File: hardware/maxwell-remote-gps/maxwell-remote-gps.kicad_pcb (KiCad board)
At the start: 2 copper layers, 52 x 21.5 mm, 11 parts, among them J1 IO, J2 UART1, U1 SC16IS752IPW, U2 FGPMMOPA6C, Y1 14.7456M

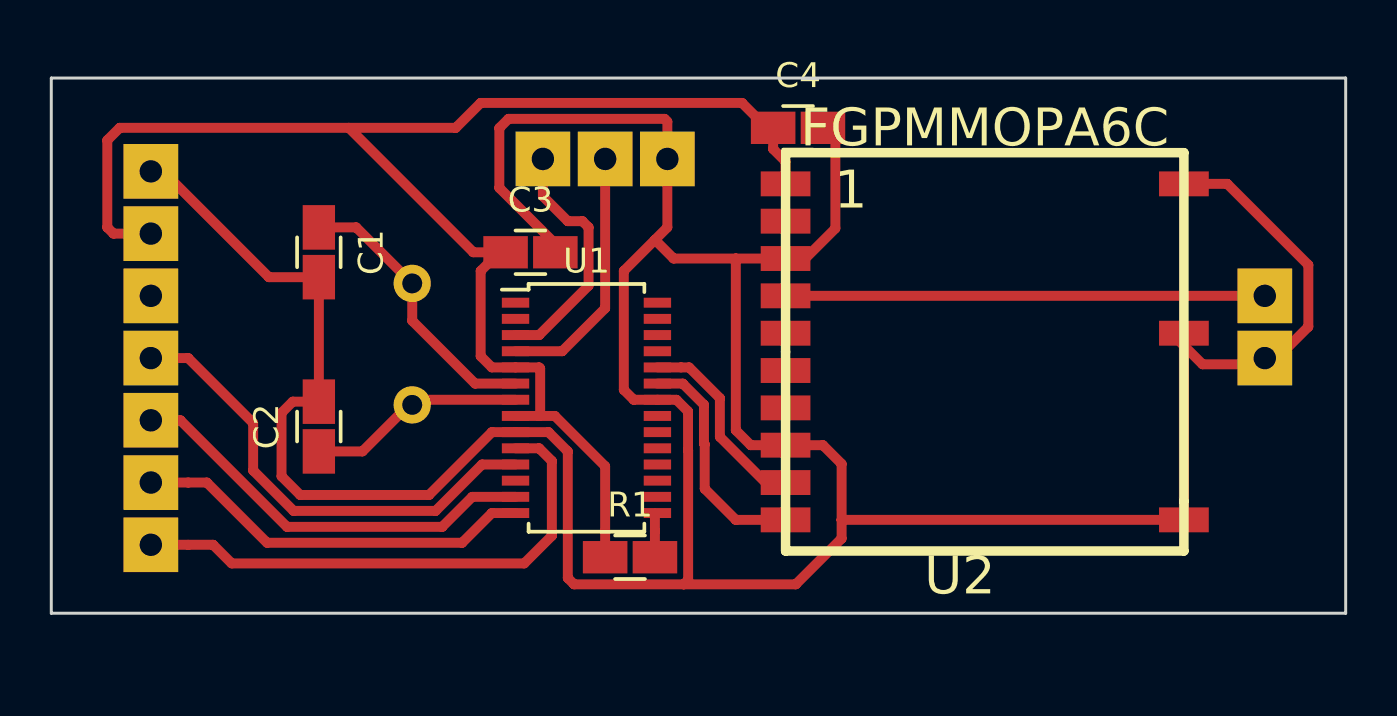
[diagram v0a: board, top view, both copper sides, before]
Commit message: Updating to include possible GPIOs for PPS and 3DFIX.
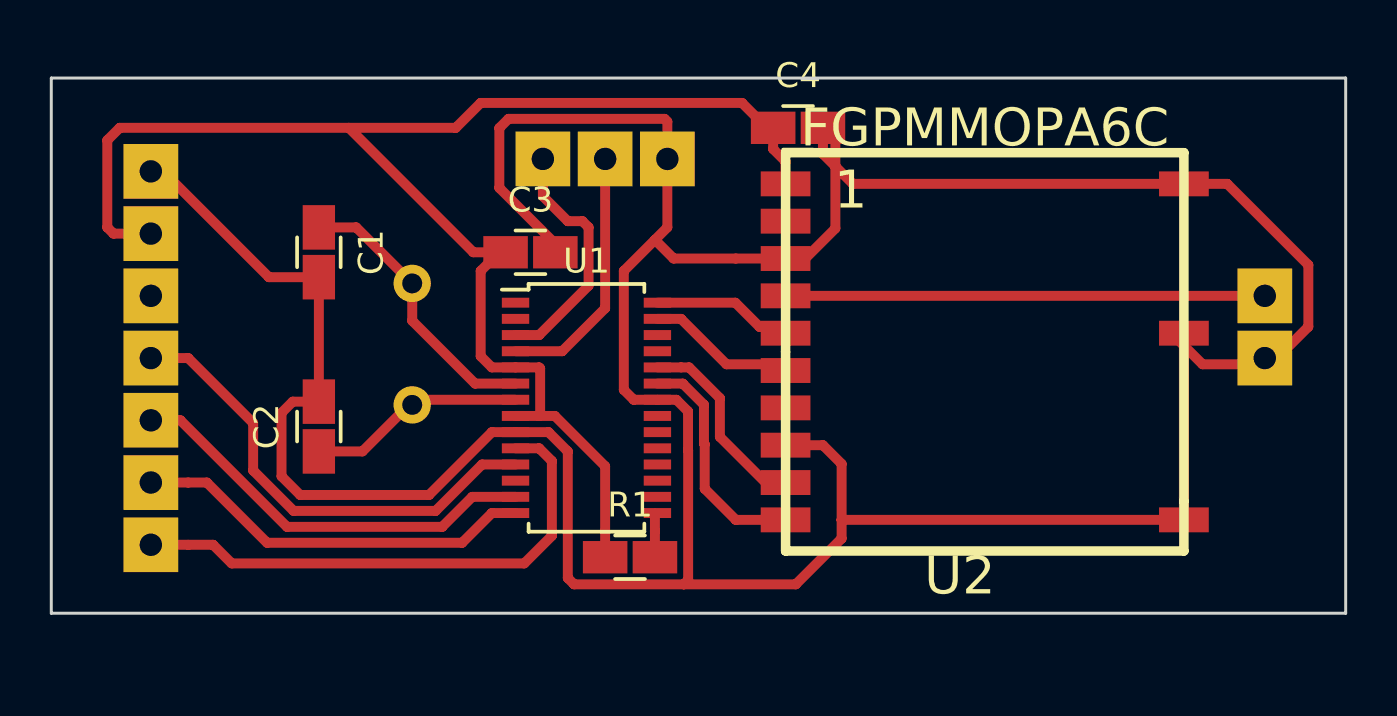
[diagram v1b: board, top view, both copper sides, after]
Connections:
- U1 pad 27: (no net) -> Net-(U1-Pad27)
- U1 pad 28: (no net) -> Net-(U1-Pad28)
- U2 pad 5: (no net) -> Net-(U1-Pad28)
- U2 pad 6: (no net) -> Net-(U1-Pad27)
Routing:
- net GND: track 147.6 -> 154.5 mm
- net Net-(U1-Pad27): track 0.00 -> 5.91 mm
- net Net-(U1-Pad28): track 0.00 -> 5.55 mm
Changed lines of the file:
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@@
     (thickness 1.6)
     (drawings 4)
-    (tracks 155)
+    (tracks 161)
     (zones 0)
     (modules 11)
-    (nets 15)
+    (nets 17)
   )
   (page A4)
@@
   (net 13 "Net-(J2-Pad2)")
   (net 14 "Net-(J2-Pad1)")
+  (net 15 "Net-(U1-Pad28)")
+  (net 16 "Net-(U1-Pad27)")
   (net_class Default "This is the default net class."
     (clearance 0.24)
@@
     (add_net "Net-(U1-Pad23)")
     (add_net "Net-(U1-Pad24)")
+    (add_net "Net-(U1-Pad27)")
+    (add_net "Net-(U1-Pad28)")
     (add_net SCK)
   )
@@
       (net 1 GND))
     (pad 7 smd rect (at -8.001 2.25044) (size 1.99898 1.00076) (layers F.Cu F.Paste F.Mask))
-    (pad 6 smd rect (at -8.001 0.7493) (size 1.99898 1.00076) (layers F.Cu F.Paste F.Mask))
-    (pad 5 smd rect (at -8.001 -0.7493) (size 1.99898 1.00076) (layers F.Cu F.Paste F.Mask))
+    (pad 6 smd rect (at -8.001 0.7493) (size 1.99898 1.00076) (layers F.Cu F.Paste F.Mask)
+      (net 16 "Net-(U1-Pad27)"))
+    (pad 5 smd rect (at -8.001 -0.7493) (size 1.99898 1.00076) (layers F.Cu F.Paste F.Mask)
+      (net 15 "Net-(U1-Pad28)"))
     (pad 4 smd rect (at -8.001 -2.25044) (size 1.99898 1.00076) (layers F.Cu F.Paste F.Mask)
       (net 2 "Net-(BT1-Pad1)"))
@@
     (fp_line (start 2.2 -4.85) (end 2.2 4.85) (layer F.Fab) (width 0.15))
     (fp_line (start -1.2 -4.85) (end 2.2 -4.85) (layer F.Fab) (width 0.15))
-    (pad 28 smd rect (at 2.85 -4.225) (size 1.1 0.4) (layers F.Cu F.Paste F.Mask))
-    (pad 27 smd rect (at 2.85 -3.575) (size 1.1 0.4) (layers F.Cu F.Paste F.Mask))
+    (pad 28 smd rect (at 2.85 -4.225) (size 1.1 0.4) (layers F.Cu F.Paste F.Mask)
+      (net 15 "Net-(U1-Pad28)"))
+    (pad 27 smd rect (at 2.85 -3.575) (size 1.1 0.4) (layers F.Cu F.Paste F.Mask)
+      (net 16 "Net-(U1-Pad27)"))
     (pad 26 smd rect (at 2.85 -2.925) (size 1.1 0.4) (layers F.Cu F.Paste F.Mask))
     (pad 25 smd rect (at 2.85 -2.275) (size 1.1 0.4) (layers F.Cu F.Paste F.Mask))
@@
   (segment (start 175.5 93.025) (end 175.5 88.25) (width 0.4) (layer F.Cu) (net 1))
   (segment (start 177.50096 87.75096) (end 176.75 87) (width 0.4) (layer F.Cu) (net 1))
-  (segment (start 180.59951 95.24904) (end 180 94.64953) (width 0.4) (layer F.Cu) (net 1))
-  (segment (start 181.999 95.24904) (end 180.59951 95.24904) (width 0.4) (layer F.Cu) (net 1))
   (segment (start 178.085001 100.664999) (end 177.909999 100.840001) (width 0.4) (layer F.Cu) (net 1))
   (segment (start 178.079967 93.890191) (end 178.079968 95.444834) (width 0.4) (layer F.Cu) (net 1))
@@
   (segment (start 178.079968 95.444834) (end 178.085001 95.449867) (width 0.4) (layer F.Cu) (net 1))
   (segment (start 177.614776 93.425) (end 178.079967 93.890191) (width 0.4) (layer F.Cu) (net 1))
-  (segment (start 180 94.64953) (end 180 87.75096) (width 0.4) (layer F.Cu) (net 1))
   (segment (start 181.999 87.75096) (end 180 87.75096) (width 0.4) (layer F.Cu) (net 1))
   (segment (start 180 87.75096) (end 177.50096 87.75096) (width 0.4) (layer F.Cu) (net 1))
@@
   (segment (start 172.75 87.5) (end 172.75 87.162998) (width 0.4) (layer F.Cu) (net 1))
   (segment (start 170.5 84.912998) (end 170.5 82.507998) (width 0.4) (layer F.Cu) (net 1))
+  (segment (start 184.70122 84.75122) (end 183.5 83.55) (width 0.4) (layer F.Cu) (net 1))
+  (segment (start 198.001 84.75122) (end 184.70122 84.75122) (width 0.4) (layer F.Cu) (net 1))
+  (segment (start 183.5 83.55) (end 183.5 82.5) (width 0.4) (layer F.Cu) (net 1))
   (segment (start 181.999 89.24956) (end 201.24956 89.24956) (width 0.4) (layer F.Cu) (net 2))
   (segment (start 201.24956 89.24956) (end 201.25 89.25) (width 0.4) (layer F.Cu) (net 2))
@@
   (segment (start 173.837002 86.25) (end 173.25 86.25) (width 0.4) (layer F.Cu) (net 14))
   (segment (start 173.25 86.25) (end 172.25 85.25) (width 0.4) (layer F.Cu) (net 14))
+  (segment (start 179.982568 89.525) (end 180.957568 90.5) (width 0.4) (layer F.Cu) (net 15))
+  (segment (start 176.85 89.525) (end 179.982568 89.525) (width 0.4) (layer F.Cu) (net 15))
+  (segment (start 180.957568 90.5) (end 182 90.5) (width 0.4) (layer F.Cu) (net 15))
+  (segment (start 177.8 90.175) (end 179.625 92) (width 0.4) (layer F.Cu) (net 16))
+  (segment (start 176.85 90.175) (end 177.8 90.175) (width 0.4) (layer F.Cu) (net 16))
+  (segment (start 179.625 92) (end 182 92) (width 0.4) (layer F.Cu) (net 16))
 )

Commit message: Updating maxwell-remote-gps to latest schematic and layout.
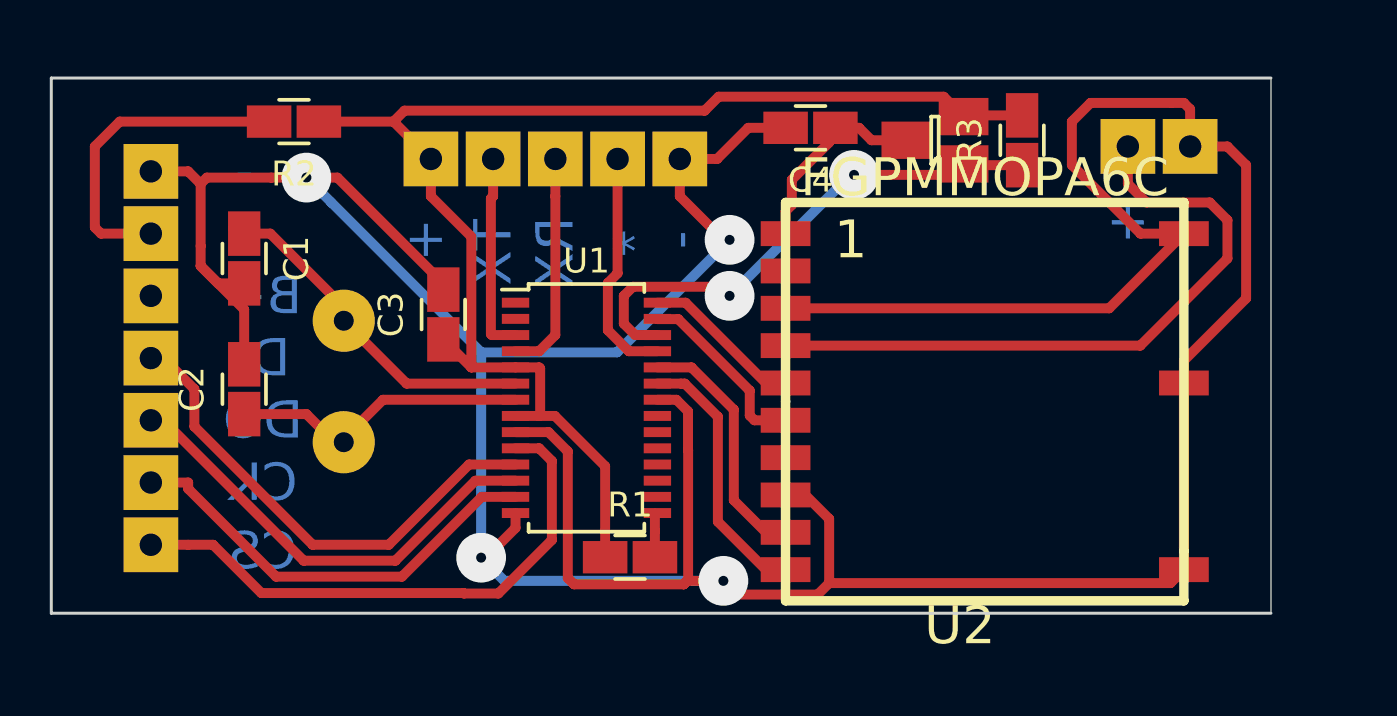
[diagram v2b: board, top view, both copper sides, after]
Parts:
- added Q1: NTR1P02T1, coddingtonbear:SOT-23_LargePads, F.Cu at (188.0, 83.0)
- added R2: 0, coddingtonbear:0805_Milling, F.Cu at (162.2, 82.2)
- added R3: 10k, coddingtonbear:0805_Milling, F.Cu at (191.5, 83.0)
- J2: value UART1 -> UART-A; footprint coddingtonbear:JST_EH_B03B-EH-A_03x2.50mm_Straight_LargePads -> coddingtonbear:JST_EH_B05B-EH-A_05x2.50mm_Straight_LargePads
- Y1: footprint Crystal:Crystal_HC49-U_Vertical -> coddingtonbear:Crystal_HC49-U_Vertical_LargePads
- moved BT1 8.14 mm to (195.8, 83.2), turned to 0 degrees
- moved J2 4.50 mm to (167.8, 83.8)
- moved C3 4.30 mm to (168.2, 90.0), turned to 90 degrees
- moved C2 3.35 mm to (160.2, 93.0)
- moved Y1 3.13 mm to (164.2, 90.2)
- moved C1 3.01 mm to (160.2, 87.8)
- moved U2 2.00 mm to (190.0, 93.5)
- moved C4 0.50 mm to (183.0, 82.5), turned to 180 degrees
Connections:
- net Net-(BT1-Pad1) renamed /VBACKUP
- net Net-(U1-Pad23) renamed /TX-B
- net Net-(U1-Pad24) renamed /RX-B
- net Net-(U1-Pad27) renamed /3DFIX(GPIO6)
- net Net-(U1-Pad28) renamed /1PPS(GPIO7)
- C4 pad 1: +3V3 -> Net-(C4-Pad1)
- J1 pad 6: +3V3 -> Net-(J1-Pad6)
- J2 pad 1: Net-(J2-Pad1) -> +3V3
- J2 pad 2: Net-(J2-Pad2) -> /TX-A
- J2 pad 3: GND -> /RX-A
- U1 pad 12: (no net) -> MISO
- U1 pad 13: MISO -> SCK
- U1 pad 14: SCK -> GND
- U1 pad 25: (no net) -> /GPIO5
- U1 pad 26: (no net) -> ~EN_GPS
- U1 pad 3: Net-(J2-Pad1) -> /TX-A
- U1 pad 4: Net-(J2-Pad2) -> /RX-A
- U2 pad 1: +3V3 -> Net-(C4-Pad1)
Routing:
- net ~EN_GPS: track 0.00 -> 21.1 mm, vias 0 -> 2
- net GND: track 154.5 -> 173.6 mm, vias 0 -> 4
- net Net-(J1-Pad6): track 0.00 -> 13.0 mm
- net Net-(J2-Pad2): track 10.3 -> 0.00 mm
- net Net-(J2-Pad1): track 9.95 -> 0.00 mm
- net /GPIO5: track 0.00 -> 9.63 mm
- net /RX-A: track 0.00 -> 8.94 mm
- net /TX-A: track 0.00 -> 8.08 mm
- net Net-(C4-Pad1): track 0.00 -> 8.03 mm
- net /VBACKUP: track 19.3 -> 26.8 mm
- net +3V3: track 61.1 -> 55.0 mm
- net Net-(C2-Pad1): track 8.51 -> 12.2 mm
- net Net-(C1-Pad1): track 11.4 -> 13.7 mm
- net /RX-B: track 7.98 -> 10.0 mm
- net SCK: track 16.1 -> 17.7 mm
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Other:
- board size 52 x 21.5 mm -> 49 x 21.5 mm
- net class Default: via_dia 0.8 -> 2
- board text added: "*"
- board text added: "+"
- board text added: "-"
- board text added: "B+"
- board text added: "CK"
- board text added: "CS"
- board text added: "DI"
- board text added: "DO"
- board text added: "RX"
- board text added: "TX"
